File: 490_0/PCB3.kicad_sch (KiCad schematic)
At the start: 7 parts, among them J13 S2B-ZR, J14 Conn_01x10, J22 2000-1-1-20-00-BK, J8 0522711579, U12 TPD8S009DSMR

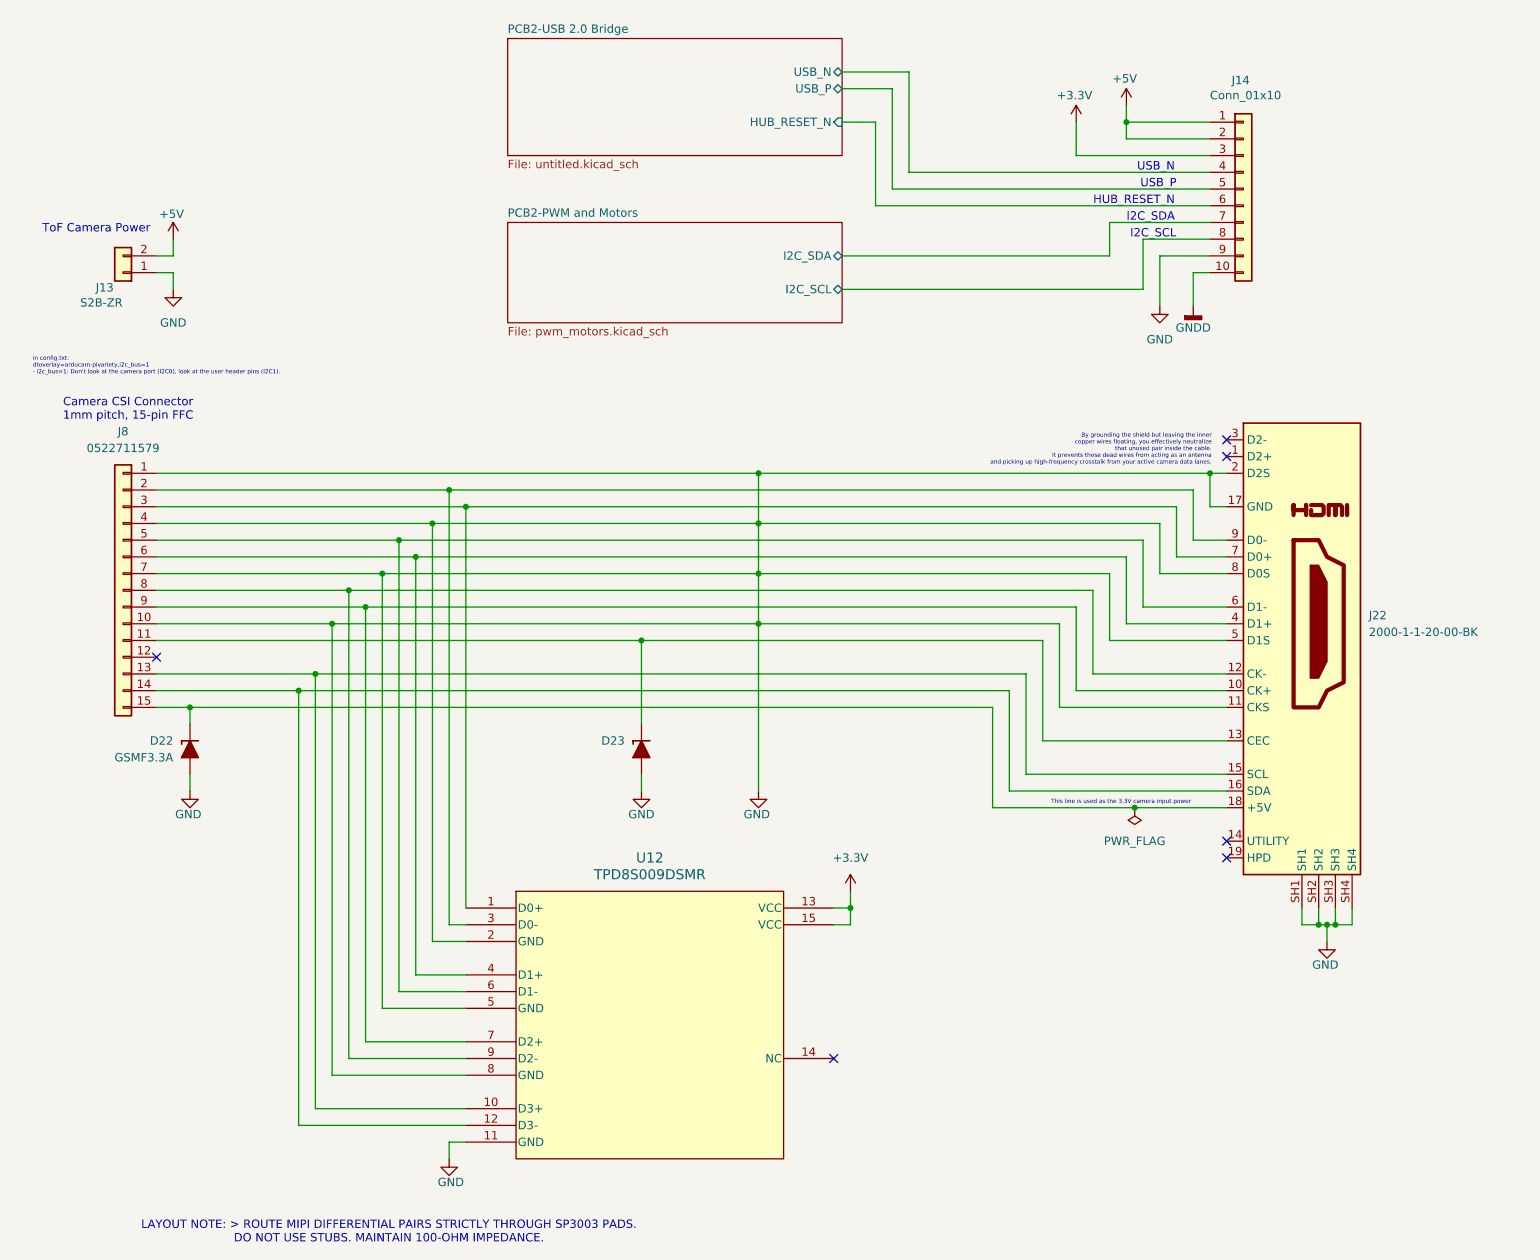
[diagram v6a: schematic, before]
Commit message: changed power and ground symbols for glasses
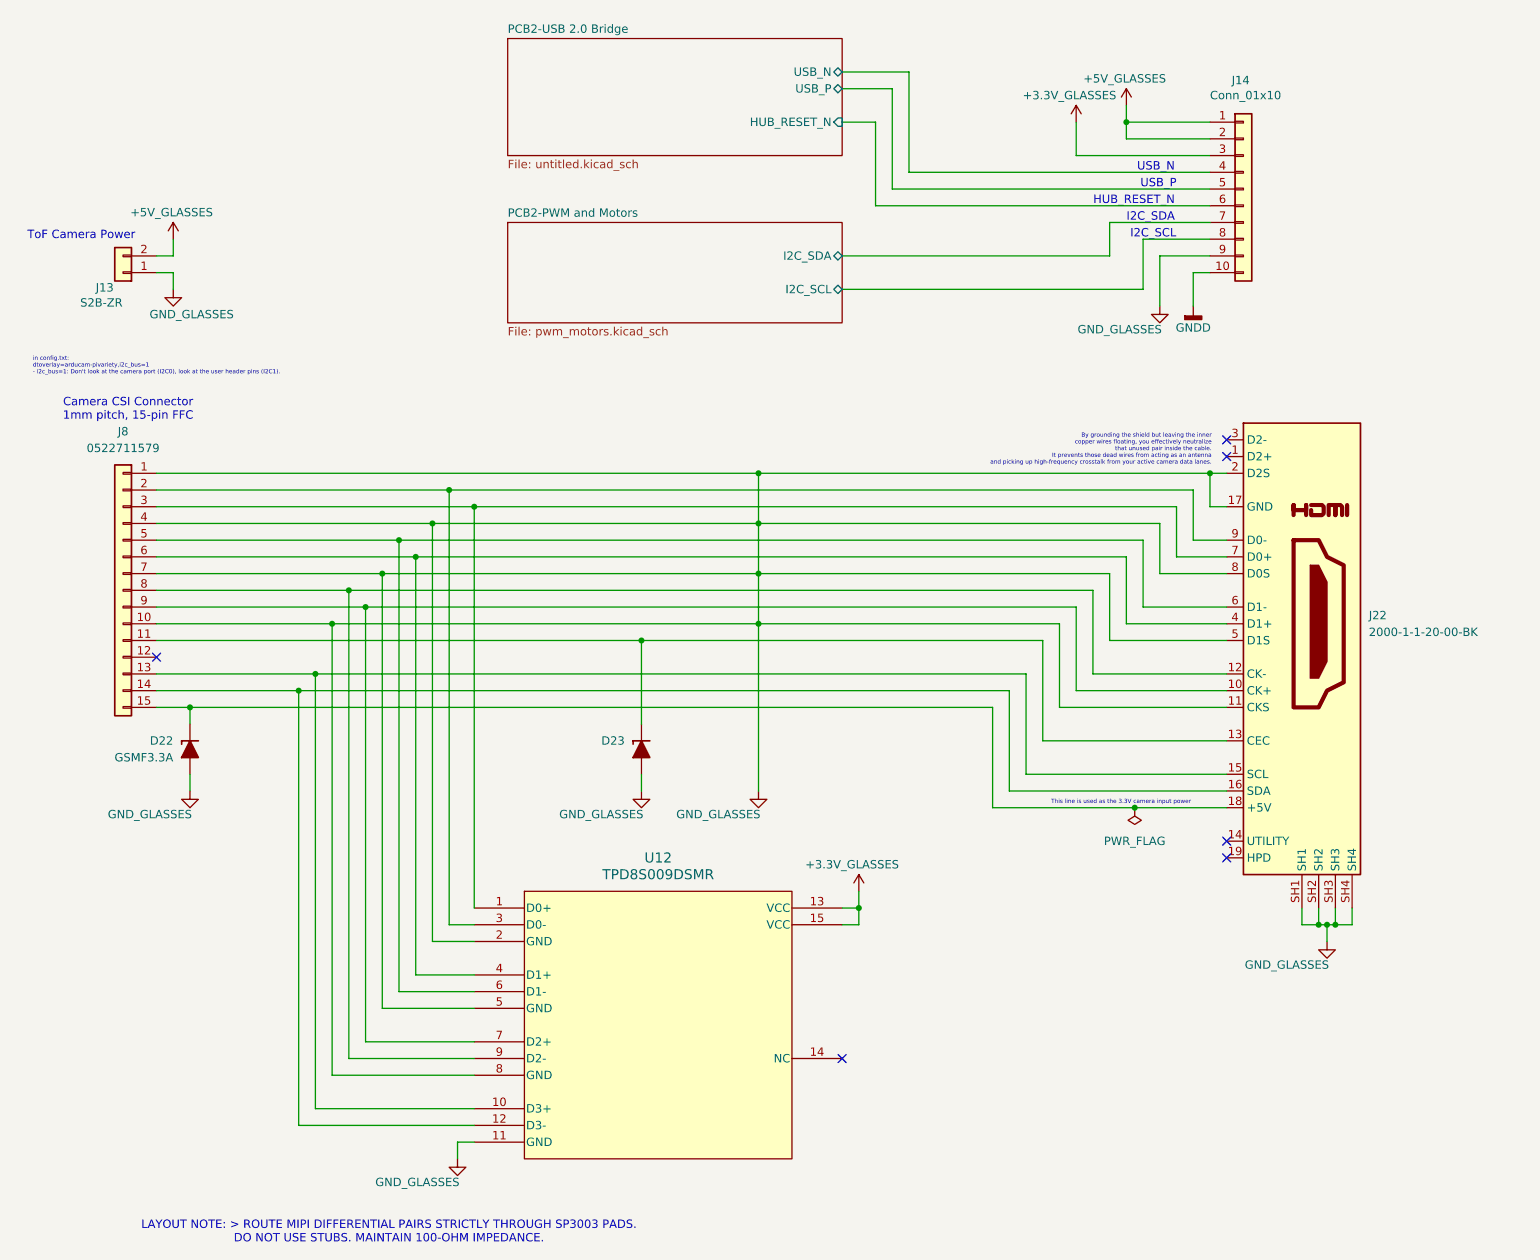
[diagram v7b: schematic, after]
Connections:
- net +3.3V renamed +3.3V_GLASSES
- net +5V renamed +5V_GLASSES
- net GND renamed GND_GLASSES
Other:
- moved on the sheet: U12

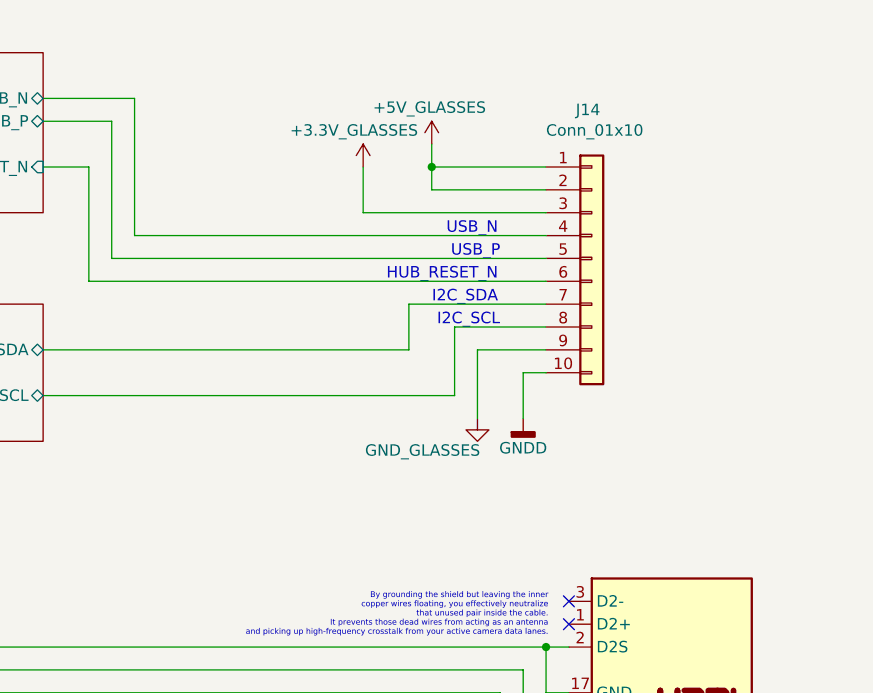
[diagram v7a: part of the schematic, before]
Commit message: ERC check fix
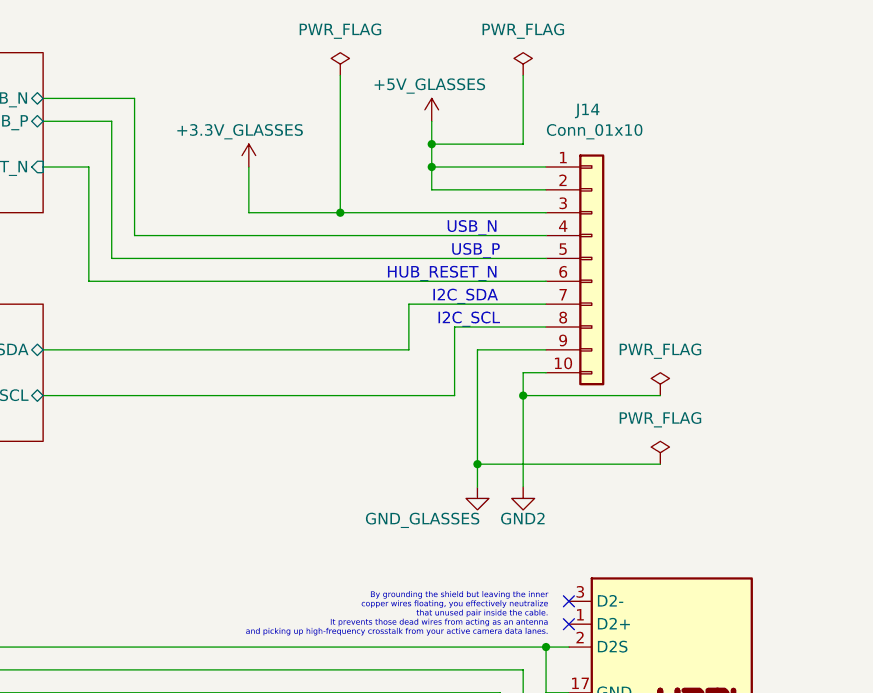
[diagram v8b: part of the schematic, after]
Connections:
- net GNDD renamed GND2
